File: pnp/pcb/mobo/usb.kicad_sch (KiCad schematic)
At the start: 4 parts, among them J9 USB_B, U5 SRL05

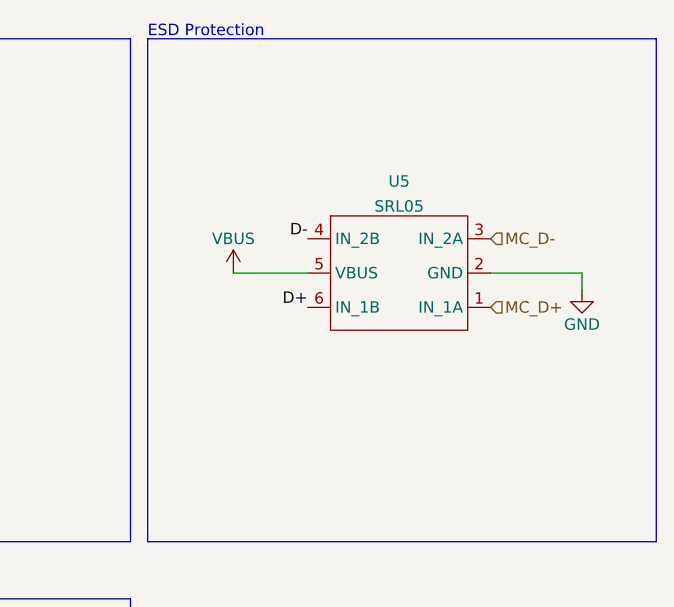
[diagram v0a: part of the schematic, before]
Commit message: replaces SRL05 for SRV05 due to pricing and availability, routed mostfet gate resistors and added 2g34 buffer to boost the voltage of the servo drive pins. consolidated a random cap value that could be switched to an existing one.
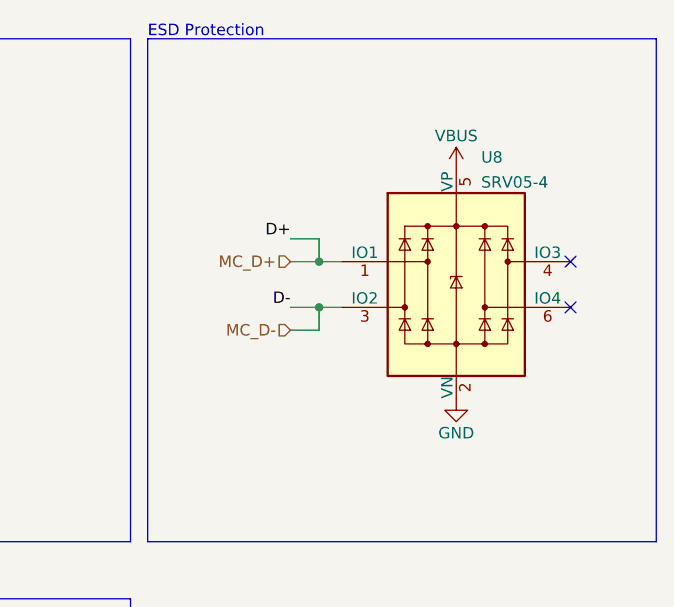
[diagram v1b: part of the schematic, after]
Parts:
- removed U5: SRL05, Package_TO_SOT_SMD:SOT-23-6, symbol index:SRL05
- added U8: SRV05-4, Package_TO_SOT_SMD:SOT-23-6, symbol Power_Protection:SRV05-4
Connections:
- net D+ is gone; now on net MC_D+: J9.3 (D+), TP2.1
- net D- is gone; now on net MC_D-: J9.2 (D-), TP1.1
- net GND: now also U8.2 (VN)
- net MC_D+: now also U8.1 (IO1)
- net MC_D-: now also U8.3 (IO2)
- net VBUS: now also U8.5 (VP)
- no-connect marks 0 -> 2
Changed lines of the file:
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@@
   (junction (at 74.93 85.725) (diameter 0) (color 0 0 0 0)
   )
+  (junction (at 128.905 76.835) (diameter 0) (color 0 0 0 0)
+  )
+  (junction (at 128.905 81.915) (diameter 0) (color 0 0 0 0)
+  )
+  (no_connect (at 156.845 76.835))
+  (no_connect (at 156.845 81.915))
   (polyline (pts (xy 107.95 52.07) (xy 107.95 107.95))
     (stroke (width 0) (type default) (color 0 0 0 0))
   )
+  (wire (pts (xy 125.73 81.915) (xy 128.905 81.915))
+    (stroke (width 0) (type default) (color 0 0 0 0))
+  )
+  (wire (pts (xy 125.73 84.455) (xy 128.905 84.455))
+    (stroke (width 0) (type default) (color 0 0 0 0))
+  )
   (polyline (pts (xy 109.855 52.07) (xy 109.855 107.95))
     (stroke (width 0) (type default) (color 0 0 0 0))
@@
     (stroke (width 0) (type default) (color 0 0 0 0))
   )
-  (wire (pts (xy 158.115 78.105) (xy 158.115 80.01))
+  (wire (pts (xy 128.905 74.295) (xy 128.905 76.835))
+    (stroke (width 0) (type default) (color 0 0 0 0))
+  )
+  (wire (pts (xy 128.905 81.915) (xy 131.445 81.915))
+    (stroke (width 0) (type default) (color 0 0 0 0))
+  )
+  (wire (pts (xy 125.73 74.295) (xy 128.905 74.295))
     (stroke (width 0) (type default) (color 0 0 0 0))
   )
@@
     (stroke (width 0) (type default) (color 0 0 0 0))
   )
+  (wire (pts (xy 128.905 84.455) (xy 128.905 81.915))
+    (stroke (width 0) (type default) (color 0 0 0 0))
+  )
   (polyline (pts (xy 107.95 114.3) (xy 107.95 128.27))
     (stroke (width 0) (type default) (color 0 0 0 0))
@@
     (stroke (width 0) (type default) (color 0 0 0 0))
   )
-  (wire (pts (xy 119.38 78.105) (xy 127.635 78.105))
-    (stroke (width 0) (type default) (color 0 0 0 0))
-  )
   (polyline (pts (xy 166.37 107.95) (xy 109.855 107.95))
     (stroke (width 0) (type default) (color 0 0 0 0))
   )
-  (wire (pts (xy 147.955 78.105) (xy 158.115 78.105))
+  (wire (pts (xy 128.905 76.835) (xy 131.445 76.835))
     (stroke (width 0) (type default) (color 0 0 0 0))
   )
@@
     (stroke (width 0) (type default) (color 0 0 0 0))
   )
+  (wire (pts (xy 125.73 76.835) (xy 128.905 76.835))
+    (stroke (width 0) (type default) (color 0 0 0 0))
+  )
   (polyline (pts (xy 109.855 52.07) (xy 166.37 52.07))
     (stroke (width 0) (type default) (color 0 0 0 0))
@@
     (effects (font (size 1.27 1.27)) (justify left bottom))
   )
+  (label "D-" (at 125.73 81.915 180)
+    (effects (font (size 1.27 1.27)) (justify right bottom))
+  )
+  (label "D+" (at 125.73 74.295 180)
+    (effects (font (size 1.27 1.27)) (justify right bottom))
+  )
   (label "D+" (at 87.63 124.46 180)
     (effects (font (size 1.27 1.27)) (justify right bottom))
@@
     (effects (font (size 1.27 1.27)) (justify left bottom))
   )
-  (label "D-" (at 127.635 74.295 180)
-    (effects (font (size 1.27 1.27)) (justify right bottom))
-  )
-  (label "D+" (at 127.635 81.915 180)
-    (effects (font (size 1.27 1.27)) (justify right bottom))
-  )
   (label "D+" (at 85.09 75.565 0)
     (effects (font (size 1.27 1.27)) (justify left bottom))
@@
     (effects (font (size 1.27 1.27)) (justify right bottom))
   )
-  (hierarchical_label "MC_D+" (shape input) (at 147.955 81.915 0)
-    (effects (font (size 1.27 1.27)) (justify left))
-  )
-  (hierarchical_label "MC_D-" (shape input) (at 147.955 74.295 0)
-    (effects (font (size 1.27 1.27)) (justify left))
+  (hierarchical_label "MC_D+" (shape input) (at 125.73 76.835 180)
+    (effects (font (size 1.27 1.27)) (justify right))
+  )
+  (hierarchical_label "MC_D-" (shape input) (at 125.73 84.455 180)
+    (effects (font (size 1.27 1.27)) (justify right))
   )
   (symbol (lib_id "Connector:TestPoint") (at 87.63 118.11 270) (unit 1)
@@
     (pin "1")
   )
-  (symbol (lib_id "index:SRL05") (at 137.795 78.105 0) (unit 1)
+  (symbol (lib_id "Power_Protection:SRV05-4") (at 144.145 79.375 0) (unit 1)
     (in_bom yes) (on_board yes) (fields_autoplaced)
-    (property "Reference" "U5" (id 0) (at 137.795 67.9155 0))
-    (property "Value" "SRL05" (id 1) (at 137.795 70.6906 0))
-    (property "Footprint" "Package_TO_SOT_SMD:SOT-23-6" (id 2) (at 147.955 78.105 90)
-      (effects (font (size 1.27 1.27)) hide)
-    )
-    (property "Datasheet" "" (id 3) (at 147.955 78.105 90)
+    (property "Reference" "U8" (id 0) (at 146.9137 65.2485 0)
+      (effects (font (size 1.27 1.27)) (justify left))
+    )
+    (property "Value" "SRV05-4" (id 1) (at 146.9137 68.0236 0)
+      (effects (font (size 1.27 1.27)) (justify left))
+    )
+    (property "Footprint" "Package_TO_SOT_SMD:SOT-23-6" (id 2) (at 161.925 90.805 0)
+      (effects (font (size 1.27 1.27)) hide)
+    )
+    (property "Datasheet" "http://www.onsemi.com/pub/Collateral/SRV05-4-D.PDF" (id 3) (at 144.145 79.375 0)
       (effects (font (size 1.27 1.27)) hide)
     )
@@
     (pin "6")
   )
+  (symbol (lib_id "power:GND") (at 144.145 92.075 0) (mirror y) (unit 1)
+    (in_bom yes) (on_board yes)
+    (property "Reference" "#PWR0140" (id 0) (at 144.145 98.425 0)
+      (effects (font (size 1.27 1.27)) hide)
+    )
+    (property "Value" "GND" (id 1) (at 144.145 95.885 0))
+    (property "Footprint" "" (id 2) (at 144.145 92.075 0)
+      (effects (font (size 1.27 1.27)) hide)
+    )
+    (property "Datasheet" "" (id 3) (at 144.145 92.075 0)
+      (effects (font (size 1.27 1.27)) hide)
+    )
+    (pin "1")
+  )
   (symbol (lib_id "power:VBUS") (at 85.09 70.485 0) (unit 1)
     (in_bom yes) (on_board yes)
@@
     )
     (property "Datasheet" "" (id 3) (at 85.09 70.485 0)
-      (effects (font (size 1.27 1.27)) hide)
-    )
-    (pin "1")
-  )
-  (symbol (lib_id "power:GND") (at 158.115 80.01 0) (mirror y) (unit 1)
-    (in_bom yes) (on_board yes)
-    (property "Reference" "#PWR0118" (id 0) (at 158.115 86.36 0)
-      (effects (font (size 1.27 1.27)) hide)
-    )
-    (property "Value" "GND" (id 1) (at 158.115 83.82 0))
-    (property "Footprint" "" (id 2) (at 158.115 80.01 0)
-      (effects (font (size 1.27 1.27)) hide)
-    )
-    (property "Datasheet" "" (id 3) (at 158.115 80.01 0)
       (effects (font (size 1.27 1.27)) hide)
     )
@@
     (pin "5")
   )
-  (symbol (lib_id "power:VBUS") (at 119.38 78.105 0) (unit 1)
-    (in_bom yes) (on_board yes)
-    (property "Reference" "#PWR0108" (id 0) (at 119.38 81.915 0)
-      (effects (font (size 1.27 1.27)) hide)
-    )
-    (property "Value" "VBUS" (id 1) (at 119.38 74.295 0))
-    (property "Footprint" "" (id 2) (at 119.38 78.105 0)
-      (effects (font (size 1.27 1.27)) hide)
-    )
-    (property "Datasheet" "" (id 3) (at 119.38 78.105 0)
-      (effects (font (size 1.27 1.27)) hide)
-    )
+  (symbol (lib_id "power:VBUS") (at 144.145 66.675 0) (unit 1)
+    (in_bom yes) (on_board yes)
+    (property "Reference" "#PWR0139" (id 0) (at 144.145 70.485 0)
+      (effects (font (size 1.27 1.27)) hide)
+    )
+    (property "Value" "VBUS" (id 1) (at 144.145 62.865 0))
+    (property "Footprint" "" (id 2) (at 144.145 66.675 0)
+      (effects (font (size 1.27 1.27)) hide)
+    )
+    (property "Datasheet" "" (id 3) (at 144.145 66.675 0)
+      (effects (font (size 1.27 1.27)) hide)
+    )

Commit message: Update mobo schematic with part numbers and ratings
All parts now have part numbers for at least one reseller or manufacturer along with rating specifications.

Note: I did not update the PCB with these new properties, as it seems the PCB is a bit out of sync with the schematic.
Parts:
- J9: Digikey (none) -> SS-52300-001
- U8: Digikey (none) -> 4617-SRV05-4TR-ND; Notes (none) -> USB TVS

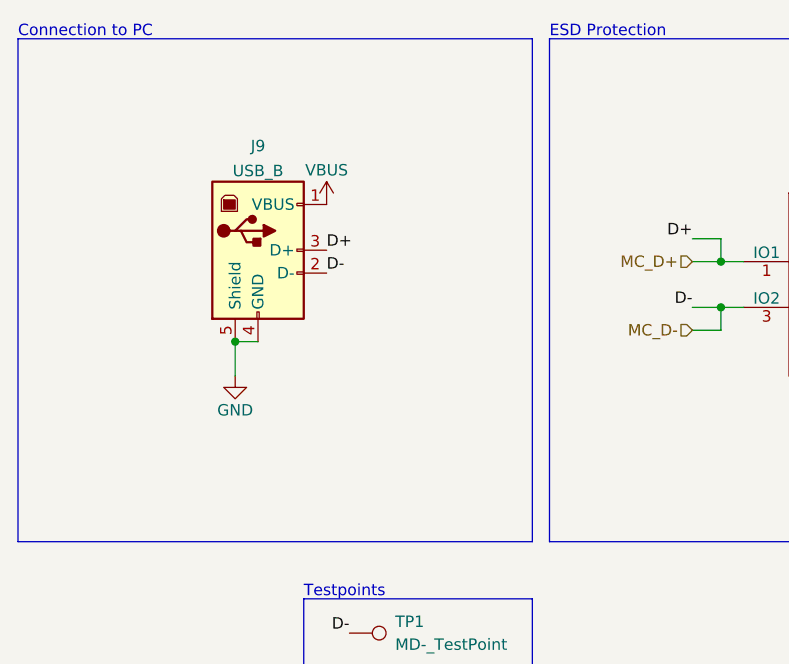
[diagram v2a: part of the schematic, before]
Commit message: adds tons of TVS and inline resistors
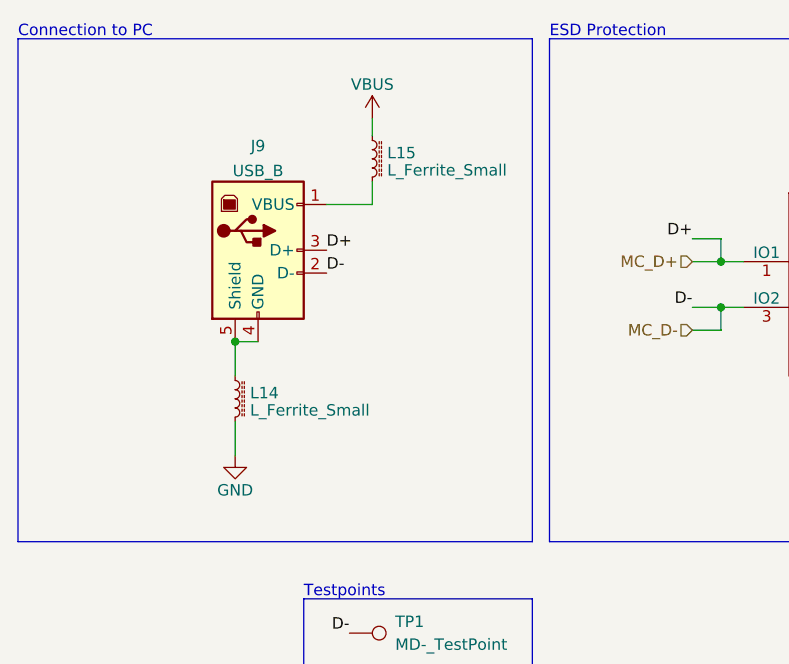
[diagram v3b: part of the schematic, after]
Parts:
- added L14, L15: L_Ferrite_Small, symbol Device:L_Ferrite_Small
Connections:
- net GND: now also L14.2; no longer J9.4 (GND), J9.5 (Shield)
- net VBUS: now also L15.1; no longer J9.1 (VBUS)
- new net: J9.1 (VBUS), L15.2
- new net: J9.4 (GND), J9.5 (Shield), L14.1
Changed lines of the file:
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@@
   (no_connect (at 156.845 76.835))
   (no_connect (at 156.845 81.915))
+  (wire (pts (xy 90.17 70.485) (xy 90.17 67.945))
+    (stroke (width 0) (type default))
+  )
   (polyline (pts (xy 107.95 52.07) (xy 107.95 107.95))
     (stroke (width 0) (type default))
@@
     (stroke (width 0) (type default))
   )
+  (wire (pts (xy 85.09 70.485) (xy 90.17 70.485))
+    (stroke (width 0) (type default))
+  )
   (wire (pts (xy 128.905 84.455) (xy 128.905 81.915))
     (stroke (width 0) (type default))
@@
     (stroke (width 0) (type default))
   )
+  (wire (pts (xy 74.93 94.615) (xy 74.93 98.425))
+    (stroke (width 0) (type default))
+  )
   (polyline (pts (xy 107.95 107.95) (xy 50.8 107.95))
     (stroke (width 0) (type default))
@@
   )
   (polyline (pts (xy 109.855 52.07) (xy 166.37 52.07))
+    (stroke (width 0) (type default))
+  )
+  (wire (pts (xy 90.17 60.96) (xy 90.17 62.865))
     (stroke (width 0) (type default))
   )
@@
     )
   )
-  (symbol (lib_id "power:GND") (at 74.93 89.535 0) (mirror y) (unit 1)
-    (in_bom yes) (on_board yes) (dnp no)
-    (property "Reference" "#PWR0136" (at 74.93 95.885 0)
-      (effects (font (size 1.27 1.27)) hide)
-    )
-    (property "Value" "GND" (at 74.93 93.345 0)
-      (effects (font (size 1.27 1.27)))
-    )
-    (property "Footprint" "" (at 74.93 89.535 0)
-      (effects (font (size 1.27 1.27)) hide)
-    )
-    (property "Datasheet" "" (at 74.93 89.535 0)
+  (symbol (lib_id "power:GND") (at 74.93 98.425 0) (mirror y) (unit 1)
+    (in_bom yes) (on_board yes) (dnp no)
+    (property "Reference" "#PWR0136" (at 74.93 104.775 0)
+      (effects (font (size 1.27 1.27)) hide)
+    )
+    (property "Value" "GND" (at 74.93 102.235 0)
+      (effects (font (size 1.27 1.27)))
+    )
+    (property "Footprint" "" (at 74.93 98.425 0)
+      (effects (font (size 1.27 1.27)) hide)
+    )
+    (property "Datasheet" "" (at 74.93 98.425 0)
       (effects (font (size 1.27 1.27)) hide)
     )
@@
     )
   )
-  (symbol (lib_id "power:VBUS") (at 85.09 70.485 0) (unit 1)
-    (in_bom yes) (on_board yes) (dnp no)
-    (property "Reference" "#PWR0138" (at 85.09 74.295 0)
-      (effects (font (size 1.27 1.27)) hide)
-    )
-    (property "Value" "VBUS" (at 85.09 66.675 0)
-      (effects (font (size 1.27 1.27)))
-    )
-    (property "Footprint" "" (at 85.09 70.485 0)
-      (effects (font (size 1.27 1.27)) hide)
-    )
-    (property "Datasheet" "" (at 85.09 70.485 0)
+  (symbol (lib_id "power:VBUS") (at 90.17 60.96 0) (unit 1)
+    (in_bom yes) (on_board yes) (dnp no)
+    (property "Reference" "#PWR0138" (at 90.17 64.77 0)
+      (effects (font (size 1.27 1.27)) hide)
+    )
+    (property "Value" "VBUS" (at 90.17 57.15 0)
+      (effects (font (size 1.27 1.27)))
+    )
+    (property "Footprint" "" (at 90.17 60.96 0)
+      (effects (font (size 1.27 1.27)) hide)
+    )
+    (property "Datasheet" "" (at 90.17 60.96 0)
       (effects (font (size 1.27 1.27)) hide)
     )
@@
     )
   )
+  (symbol (lib_id "Device:L_Ferrite_Small") (at 90.17 65.405 0) (unit 1)
+    (in_bom yes) (on_board yes) (dnp no) (fields_autoplaced)
+    (property "Reference" "L15" (at 91.821 64.7613 0)
+      (effects (font (size 1.27 1.27)) (justify left))
+    )
+    (property "Value" "L_Ferrite_Small" (at 91.821 66.6823 0)
+      (effects (font (size 1.27 1.27)) (justify left))
+    )
+    (property "Footprint" "" (at 90.17 65.405 0)
+      (effects (font (size 1.27 1.27)) hide)
+    )
+    (property "Datasheet" "~" (at 90.17 65.405 0)
+      (effects (font (size 1.27 1.27)) hide)
+    )
+    (pin "1")
+    (pin "2")
+    (instances
+      (project "mobo"
+        (path "/7255cbd1-8d38-4545-be9a-7fc5488ef942/00000000-0000-0000-0000-00005eb0c6b9"
+          (reference "L15") (unit 1)
+        )
+      )
+    )
+  )
   (symbol (lib_id "power:VBUS") (at 144.145 66.675 0) (unit 1)
     (in_bom yes) (on_board yes) (dnp no)
@@
         )
       )
+    )
+  )
+  (symbol (lib_id "Device:L_Ferrite_Small") (at 74.93 92.075 0) (unit 1)
+    (in_bom yes) (on_board yes) (dnp no) (fields_autoplaced)
+    (property "Reference" "L14" (at 76.581 91.4313 0)
+      (effects (font (size 1.27 1.27)) (justify left))
+    )
+    (property "Value" "L_Ferrite_Small" (at 76.581 93.3523 0)
+      (effects (font (size 1.27 1.27)) (justify left))
+    )
+    (property "Footprint" "" (at 74.93 92.075 0)
+      (effects (font (size 1.27 1.27)) hide)
+    )
+    (property "Datasheet" "~" (at 74.93 92.075 0)
+      (effects (font (size 1.27 1.27)) hide)
+    )
+    (pin "1")
+    (pin "2")
+    (instances
+      (project "mobo"
+        (path "/7255cbd1-8d38-4545-be9a-7fc5488ef942/00000000-0000-0000-0000-00005eb0c6b9"
+          (reference "L14") (unit 1)
+        )
+      )

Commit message: imports new TVS and inline resistors into pcb
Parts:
- L14, L15: footprint (none) -> index:L_0805_2012Metric
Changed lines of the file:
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@@
       (effects (font (size 1.27 1.27)) (justify left))
     )
-    (property "Footprint" "" (at 90.17 65.405 0)
+    (property "Footprint" "index:L_0805_2012Metric" (at 90.17 65.405 0)
       (effects (font (size 1.27 1.27)) hide)
     )
@@
       (effects (font (size 1.27 1.27)) (justify left))
     )
-    (property "Footprint" "" (at 74.93 92.075 0)
+    (property "Footprint" "index:L_0805_2012Metric" (at 74.93 92.075 0)
       (effects (font (size 1.27 1.27)) hide)
     )

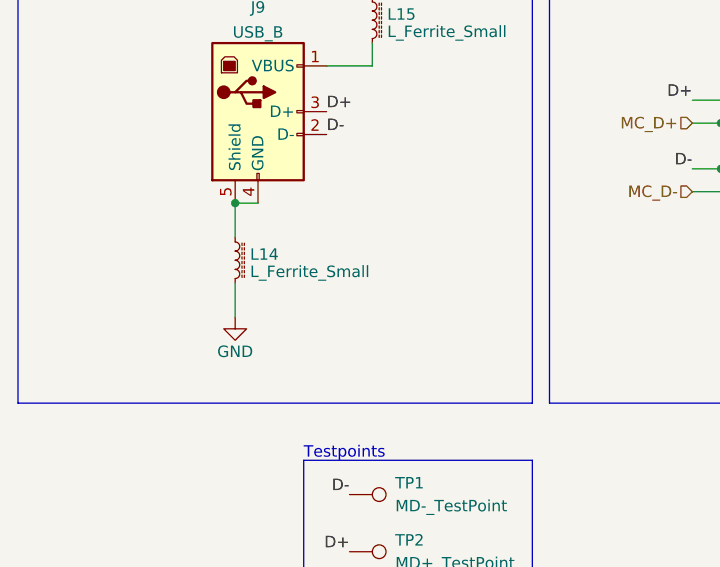
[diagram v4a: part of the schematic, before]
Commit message: Remove ferrite on USB ground
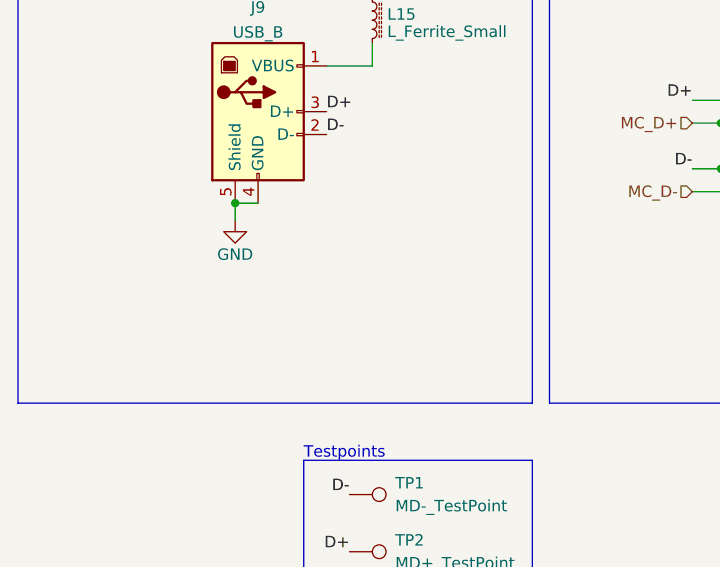
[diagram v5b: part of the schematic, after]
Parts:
- removed L14: L_Ferrite_Small, index:L_0805_2012Metric, symbol Device:L_Ferrite_Small
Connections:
- net GND: now also J9.4 (GND), J9.5 (Shield)
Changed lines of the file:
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@@
     (stroke (width 0) (type default))
   )
-  (wire (pts (xy 74.93 85.725) (xy 74.93 89.535))
+  (wire (pts (xy 74.93 85.725) (xy 74.93 87.63))
     (stroke (width 0) (type default))
   )
@@
   )
   (polyline (pts (xy 82.55 114.3) (xy 107.95 114.3))
-    (stroke (width 0) (type default))
-  )
-  (wire (pts (xy 74.93 94.615) (xy 74.93 98.425))
     (stroke (width 0) (type default))
   )
@@
     )
   )
-  (symbol (lib_id "power:GND") (at 74.93 98.425 0) (mirror y) (unit 1)
-    (in_bom yes) (on_board yes) (dnp no)
-    (property "Reference" "#PWR0136" (at 74.93 104.775 0)
-      (effects (font (size 1.27 1.27)) hide)
-    )
-    (property "Value" "GND" (at 74.93 102.235 0)
-      (effects (font (size 1.27 1.27)))
-    )
-    (property "Footprint" "" (at 74.93 98.425 0)
-      (effects (font (size 1.27 1.27)) hide)
-    )
-    (property "Datasheet" "" (at 74.93 98.425 0)
+  (symbol (lib_id "power:GND") (at 74.93 87.63 0) (mirror y) (unit 1)
+    (in_bom yes) (on_board yes) (dnp no)
+    (property "Reference" "#PWR0136" (at 74.93 93.98 0)
+      (effects (font (size 1.27 1.27)) hide)
+    )
+    (property "Value" "GND" (at 74.93 91.44 0)
+      (effects (font (size 1.27 1.27)))
+    )
+    (property "Footprint" "" (at 74.93 87.63 0)
+      (effects (font (size 1.27 1.27)) hide)
+    )
+    (property "Datasheet" "" (at 74.93 87.63 0)
       (effects (font (size 1.27 1.27)) hide)
     )
@@
         )
       )
-    )
-  )
-  (symbol (lib_id "Device:L_Ferrite_Small") (at 74.93 92.075 0) (unit 1)
-    (in_bom yes) (on_board yes) (dnp no) (fields_autoplaced)
-    (property "Reference" "L14" (at 76.581 91.4313 0)
-      (effects (font (size 1.27 1.27)) (justify left))
-    )
-    (property "Value" "L_Ferrite_Small" (at 76.581 93.3523 0)
-      (effects (font (size 1.27 1.27)) (justify left))
-    )
-    (property "Footprint" "index:L_0805_2012Metric" (at 74.93 92.075 0)
-      (effects (font (size 1.27 1.27)) hide)
-    )
-    (property "Datasheet" "~" (at 74.93 92.075 0)
-      (effects (font (size 1.27 1.27)) hide)
-    )
-    (pin "1")
-    (pin "2")
-    (instances
-      (project "mobo"
-        (path "/7255cbd1-8d38-4545-be9a-7fc5488ef942/00000000-0000-0000-0000-00005eb0c6b9"
-          (reference "L14") (unit 1)
-        )
-      )
